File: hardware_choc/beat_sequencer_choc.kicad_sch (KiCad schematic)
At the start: 6 parts, among them SW1 SW_SPST, SW74 RotaryEncoder_Switch_MP

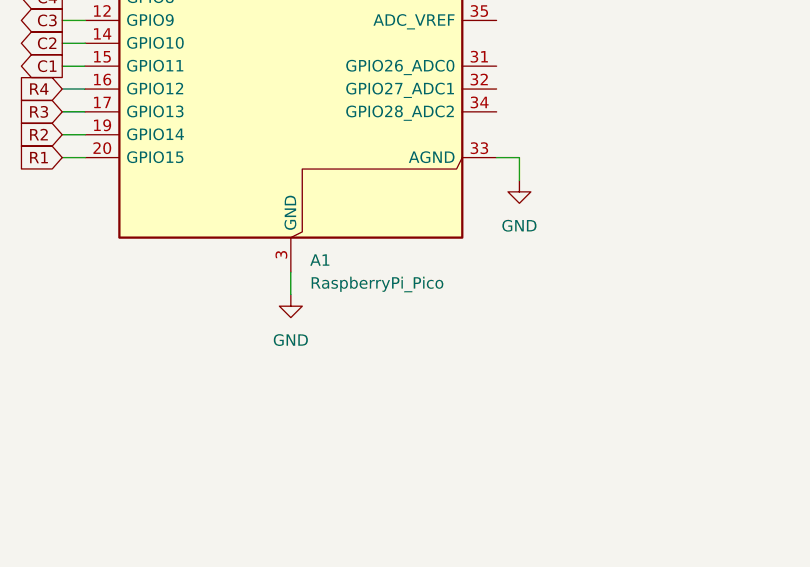
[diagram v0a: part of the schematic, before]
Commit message: Update pico partnumber
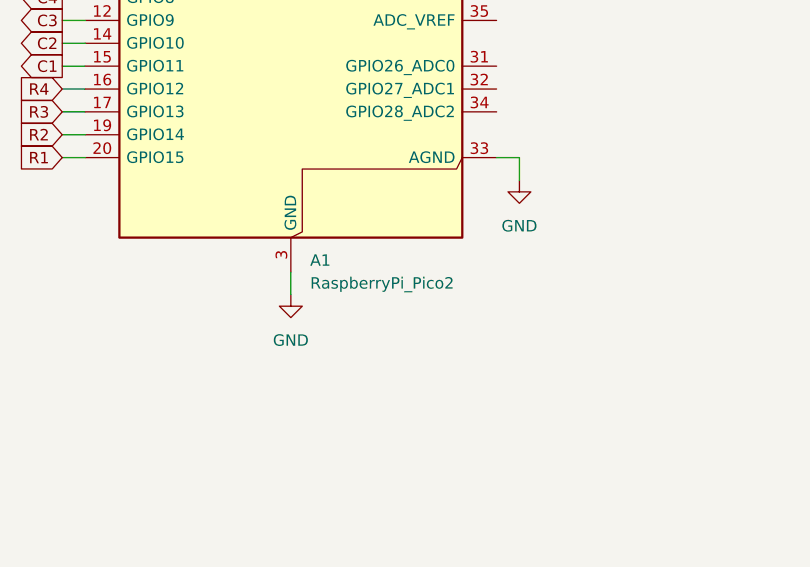
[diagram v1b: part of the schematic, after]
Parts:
- A1: value RaspberryPi_Pico -> RaspberryPi_Pico2
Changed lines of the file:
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@@
 			)
 		)
-		(property "Value" "RaspberryPi_Pico"
+		(property "Value" "RaspberryPi_Pico2"
 			(at 65.6433 116.84 0)
 			(effects
